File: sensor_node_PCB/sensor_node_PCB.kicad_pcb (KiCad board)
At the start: 2 copper layers, 97.8 x 49 mm, 47 parts, among them J1 USB_B_Mini, J3 OUTPUT_CONNECTOR, P1 BREAKOUTS, Q1 FDN340P, Q2 BSS138, Q3 BSS138, SW1 RESET_SWITCH, U1 LMV358IDGKR, U2 LD1117S50TR, U3 FT231XS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

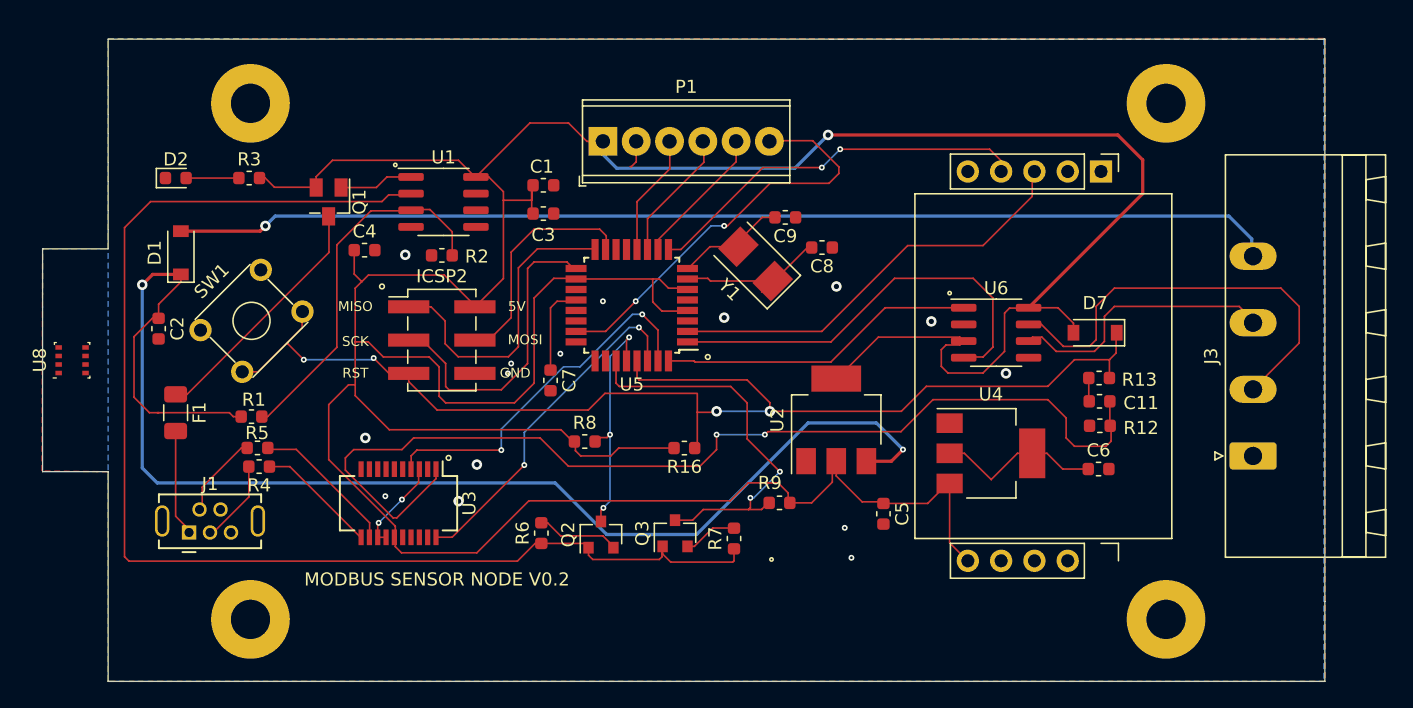
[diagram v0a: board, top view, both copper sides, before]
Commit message: put curved edges on tab
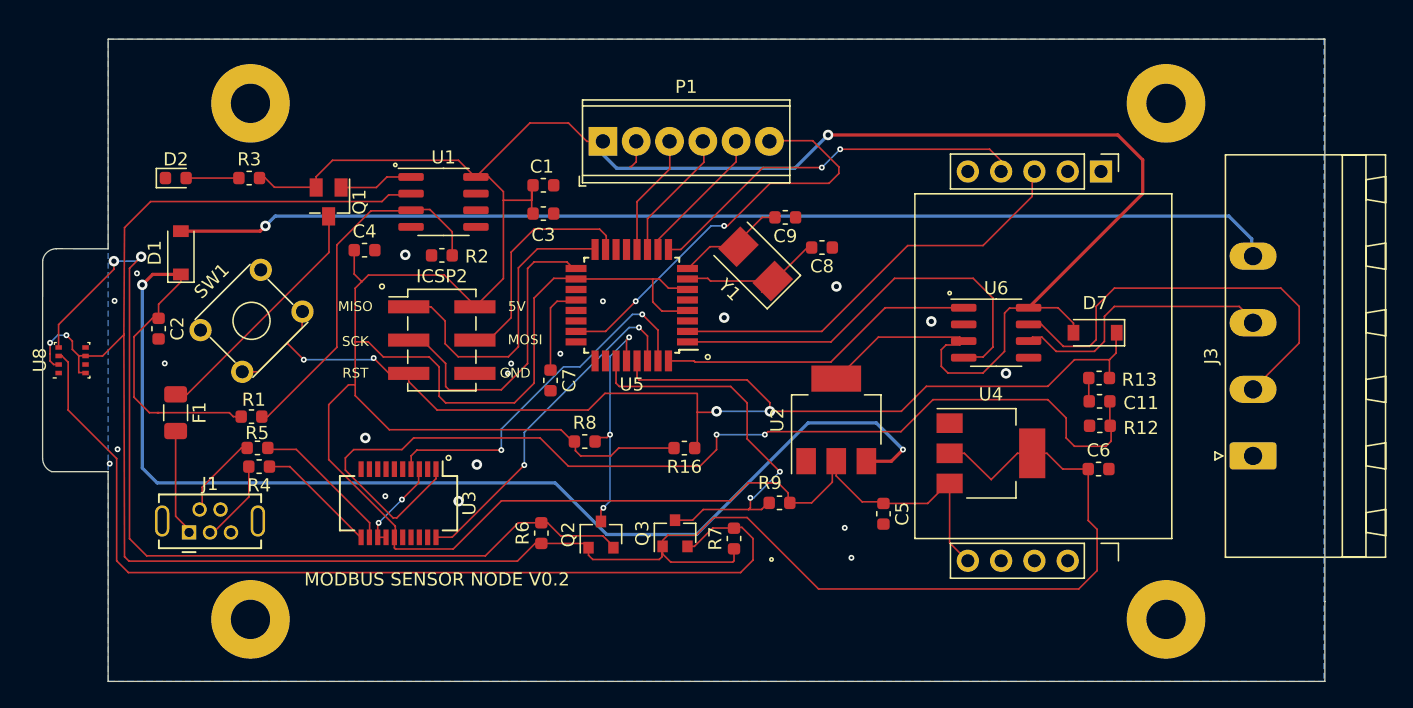
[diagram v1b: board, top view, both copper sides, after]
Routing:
- net /ARD_SDA_3V3: track 4.13 -> 74.5 mm
- net /ARD_SCL_3V3: track 6.25 -> 71.6 mm, vias 0 -> 2
- net 3V3_LDO: track 111.2 -> 167.4 mm, vias 0 -> 2
- net GND: vias 15 -> 20
- removed copper zone on F.Cu, net GND
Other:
- outline, holes or cut-outs redrawn

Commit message: replaced missing gnd plane
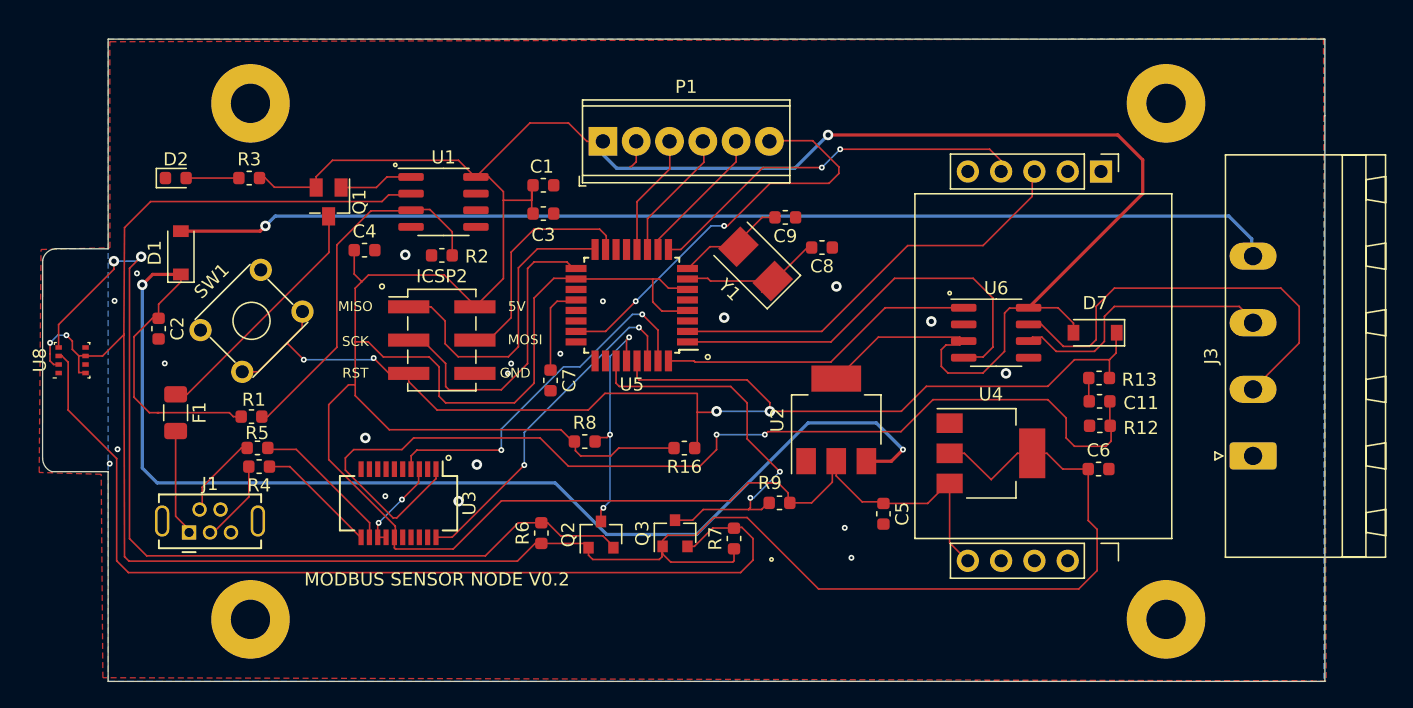
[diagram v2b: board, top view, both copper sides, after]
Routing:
- added copper zone on F.Cu, net GND
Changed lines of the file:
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@@
+    )
+  )
+  (zone (net 2) (net_name GND) (layer F.Cu) (hatch edge 0.508)
+    (connect_pads (clearance 0.254))
+    (min_thickness 0.254)
+    (fill yes (arc_segments 32) (thermal_gap 0.508) (thermal_bridge_width 0.508))
+    (polygon
+      (pts
+        (xy 200.18 132.97) (xy 106.85 132.72) (xy 106.72 117.2) (xy 101.99 117.06) (xy 102.13 100.05)
+        (xy 107.39 99.92) (xy 107.38 84.18) (xy 107.42 84.2) (xy 199.97 83.95)
+      )
     )
   )

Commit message: routed max485 en to ard d8
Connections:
- P1 pad 3: /atmega328p/ARD_DIG8 -> /atmega328p/ARD_DIG9
- U5 pad 12: /atmega328p/ARD_DIG8 -> /RS485_LINE_EN!
- U5 pad 13: Net-(U5-Pad13) -> /atmega328p/ARD_DIG9
- U6 pad 2: GND -> /RS485_LINE_EN!
- U6 pad 3: 5V_LDO -> /RS485_LINE_EN!
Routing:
- net /RS485_LINE_EN!: track 0.00 -> 36.6 mm, vias 0 -> 4
- net /atmega328p/ARD_DIG9: track 0.00 -> 9.43 mm
- net /atmega328p/ARD_DIG8: track 9.19 -> 0.00 mm
- net 5V_LDO: track 298.9 -> 292.3 mm

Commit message: added sht20 to tab
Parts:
- added U9: sht20, Package_DFN_QFN:DFN-6-1EP_3x3mm_P1mm_EP1.5x2.4mm, F.Cu at (104.9, 103.3)
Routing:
- net 3V3_LDO: track 167.4 -> 174.7 mm, vias 2 -> 3
- net /ARD_SDA_3V3: track 74.5 -> 81.7 mm
- net /ARD_SCL_3V3: track 71.6 -> 75.3 mm, vias 2 -> 4
- net GND: vias 20 -> 22
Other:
- board text added: "+12V"
- board text added: "A-"
- board text added: "B+"

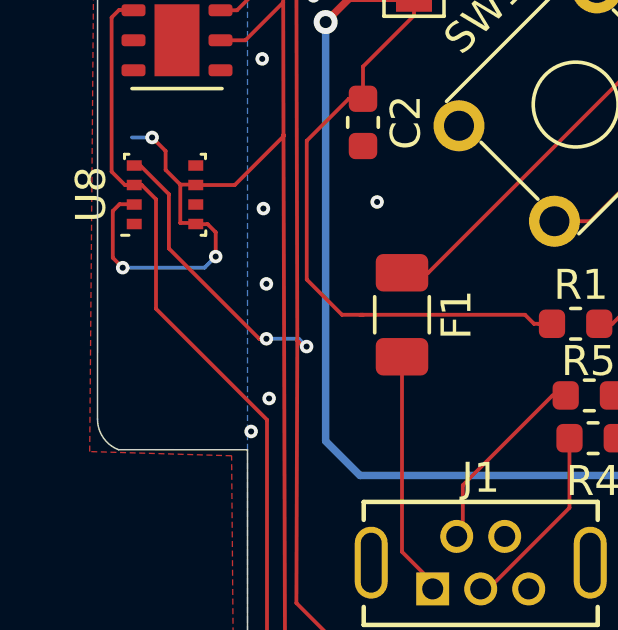
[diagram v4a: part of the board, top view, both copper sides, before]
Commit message: added dps310 to schem and board
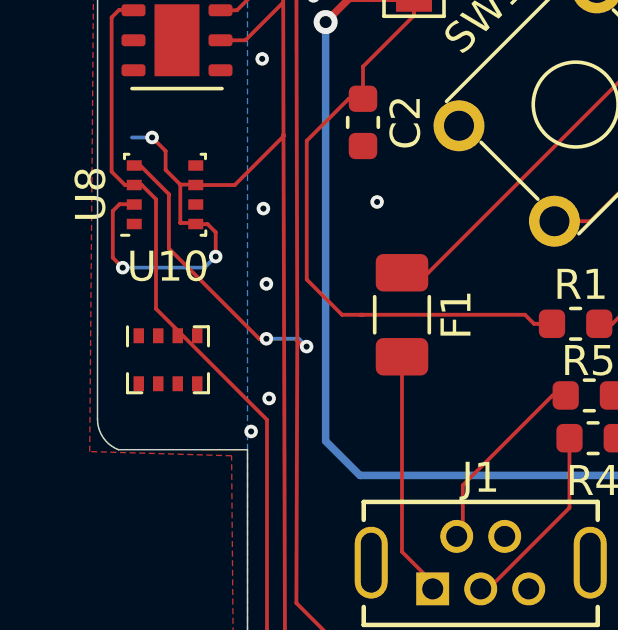
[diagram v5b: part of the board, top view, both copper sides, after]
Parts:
- added U10: dps310, Package_LGA:Bosch_LGA-8_2x2.5mm_P0.65mm_ClockwisePinNumbering, F.Cu at (104.6, 114.0)
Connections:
- U9 pad 7: GND -> Net-(U9-Pad7)
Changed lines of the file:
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@@
     (tracks 558)
     (zones 0)
-    (modules 48)
-    (nets 65)
+    (modules 49)
+    (nets 68)
   )
   (page A4)
@@
   )
   (setup
-    (last_trace_width 0.127)
+    (last_trace_width 0.25)
     (user_trace_width 0.127)
     (user_trace_width 0.5)
@@
   (net 63 "Net-(U9-Pad3)")
   (net 64 "Net-(U9-Pad4)")
+  (net 65 "Net-(U9-Pad7)")
+  (net 66 "Net-(U10-Pad5)")
+  (net 67 "Net-(U10-Pad2)")
   (net_class Default "This is the default net class."
     (clearance 0.2)
@@
     (add_net "Net-(Q1-Pad1)")
     (add_net "Net-(R1-Pad1)")
+    (add_net "Net-(U10-Pad2)")
+    (add_net "Net-(U10-Pad5)")
     (add_net "Net-(U3-Pad10)")
     (add_net "Net-(U3-Pad13)")
@@
     (add_net "Net-(U9-Pad3)")
     (add_net "Net-(U9-Pad4)")
+    (add_net "Net-(U9-Pad7)")
     (add_net USBVCC)
     (add_net Vin)
@@
       (net 23 /ARD_SCL_3V3))
     (pad 7 smd rect (at 0 0) (size 1.5 2.4) (layers F.Cu F.Mask)
-      (net 2 GND))
+      (net 65 "Net-(U9-Pad7)"))
     (pad "" smd roundrect (at -0.375 -0.6) (size 0.6 0.97) (layers F.Paste) (roundrect_rratio 0.25))
     (pad "" smd roundrect (at -0.375 0.6) (size 0.6 0.97) (layers F.Paste) (roundrect_rratio 0.25))
@@
       (at (xyz 0 0 0))
       (scale (xyz 1 1 1))
+      (rotate (xyz 0 0 0))
+    )
+  )
+  (module Package_LGA:Bosch_LGA-8_2x2.5mm_P0.65mm_ClockwisePinNumbering (layer F.Cu)
+    (at 104.6 114)
+    (descr "LGA-8, https://ae-bst.resource.bosch.com/media/_tech/media/datasheets/BST-BMP280-DS001-18.pdf")
+    (tags "lga land grid array")
+    (attr smd)
+    (fp_text reference U10 (at 0 -3.1) (layer F.SilkS)
+      (effects (font (size 1 1) (thickness 0.15)))
+    )
+    (fp_text value dps310 (at 0 3.1) (layer F.Fab)
+      (effects (font (size 1 1) (thickness 0.15)))
+    )
+    (fp_line (start -1.35 1.1) (end -0.87 1.1) (layer F.SilkS) (width 0.1))
+    (fp_text user %R (at 0 0) (layer F.Fab)
+      (effects (font (size 0.5 0.5) (thickness 0.075)))
+    )
+    (fp_line (start -1.55 -1.3) (end 1.55 -1.3) (layer F.CrtYd) (width 0.05))
+    (fp_line (start 1.55 -1.3) (end 1.55 1.3) (layer F.CrtYd) (width 0.05))
+    (fp_line (start 1.55 1.3) (end -1.55 1.3) (layer F.CrtYd) (width 0.05))
+    (fp_line (start -1.55 1.3) (end -1.55 -1.3) (layer F.CrtYd) (width 0.05))
+    (fp_line (start -1.25 1) (end 1.25 1) (layer F.Fab) (width 0.1))
+    (fp_line (start 1.25 -1) (end 1.25 1) (layer F.Fab) (width 0.1))
+    (fp_line (start 1.25 -1) (end -1 -1) (layer F.Fab) (width 0.1))
+    (fp_line (start -1 -1) (end -1.25 -0.75) (layer F.Fab) (width 0.1))
+    (fp_line (start -1.25 1) (end -1.25 -0.75) (layer F.Fab) (width 0.1))
+    (fp_line (start 0.87 1.1) (end 1.35 1.1) (layer F.SilkS) (width 0.1))
+    (fp_line (start 1.35 1.1) (end 1.35 0.46) (layer F.SilkS) (width 0.1))
+    (fp_line (start -1.35 1.1) (end -1.35 0.46) (layer F.SilkS) (width 0.1))
+    (fp_line (start 1.35 -0.46) (end 1.35 -1.1) (layer F.SilkS) (width 0.1))
+    (fp_line (start 0.87 -1.1) (end 1.35 -1.1) (layer F.SilkS) (width 0.1))
+    (fp_line (start -1.35 -0.46) (end -1.35 -1.1) (layer F.SilkS) (width 0.1))
+    (pad 1 smd rect (at -0.975 -0.8 90) (size 0.5 0.35) (layers F.Cu F.Paste F.Mask)
+      (net 2 GND))
+    (pad 5 smd rect (at 0.975 0.8 90) (size 0.5 0.35) (layers F.Cu F.Paste F.Mask)
+      (net 66 "Net-(U10-Pad5)"))
+    (pad 6 smd rect (at 0.325 0.8 90) (size 0.5 0.35) (layers F.Cu F.Paste F.Mask)
+      (net 4 3V3_LDO))
+    (pad 7 smd rect (at -0.325 0.8 90) (size 0.5 0.35) (layers F.Cu F.Paste F.Mask)
+      (net 2 GND))
+    (pad 4 smd rect (at 0.975 -0.8 90) (size 0.5 0.35) (layers F.Cu F.Paste F.Mask)
+      (net 23 /ARD_SCL_3V3))
+    (pad 3 smd rect (at 0.325 -0.8 90) (size 0.5 0.35) (layers F.Cu F.Paste F.Mask)
+      (net 26 /ARD_SDA_3V3))
+    (pad 2 smd rect (at -0.325 -0.8 90) (size 0.5 0.35) (layers F.Cu F.Paste F.Mask)
+      (net 67 "Net-(U10-Pad2)"))
+    (pad 8 smd rect (at -0.975 0.8 90) (size 0.5 0.35) (layers F.Cu F.Paste F.Mask)
+      (net 4 3V3_LDO))
+    (model ${KISYS3DMOD}/Package_LGA.3dshapes/Bosch_LGA-8_2x2.5mm_P0.65mm_ClockwisePinNumbering.wrl
+      (at (xyz 0 0 0))
+      (scale (xyz 1 1 1))

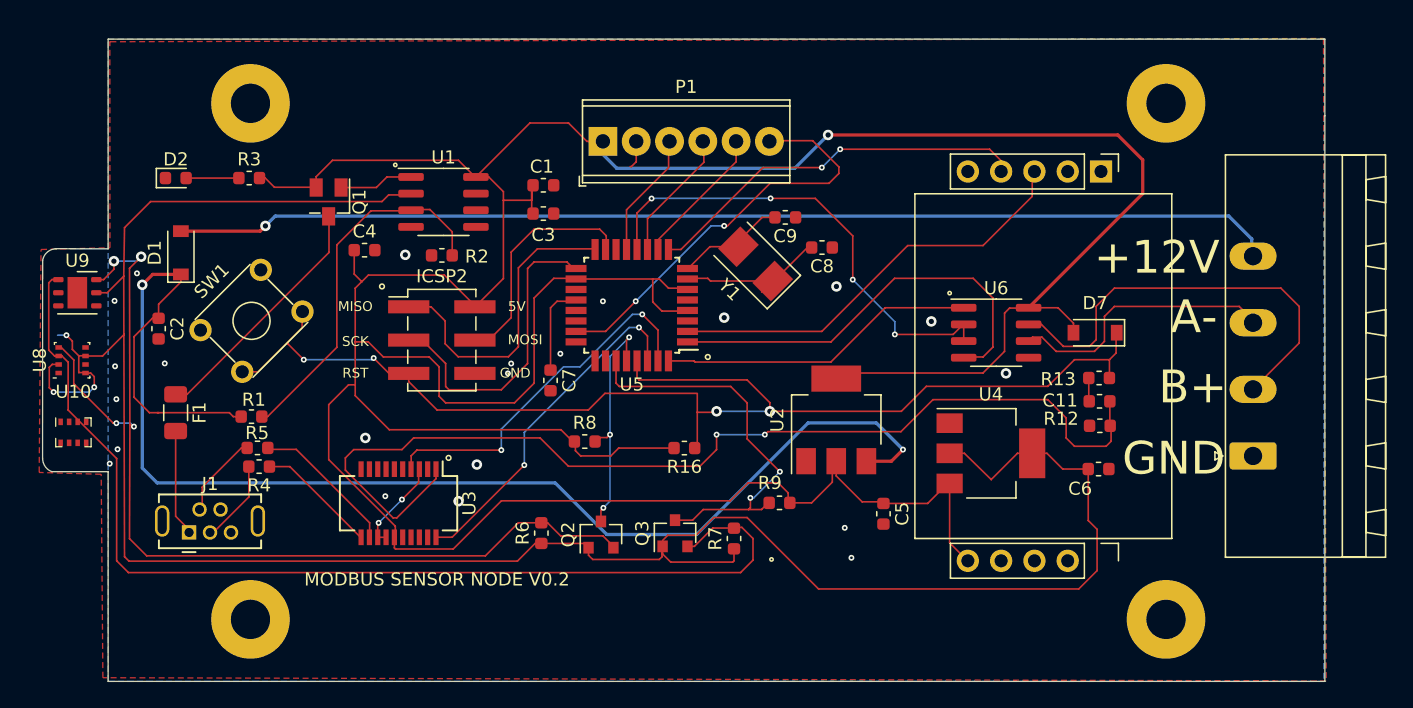
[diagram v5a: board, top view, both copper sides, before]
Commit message: changed term block to 5.08mm - added silk pin labels
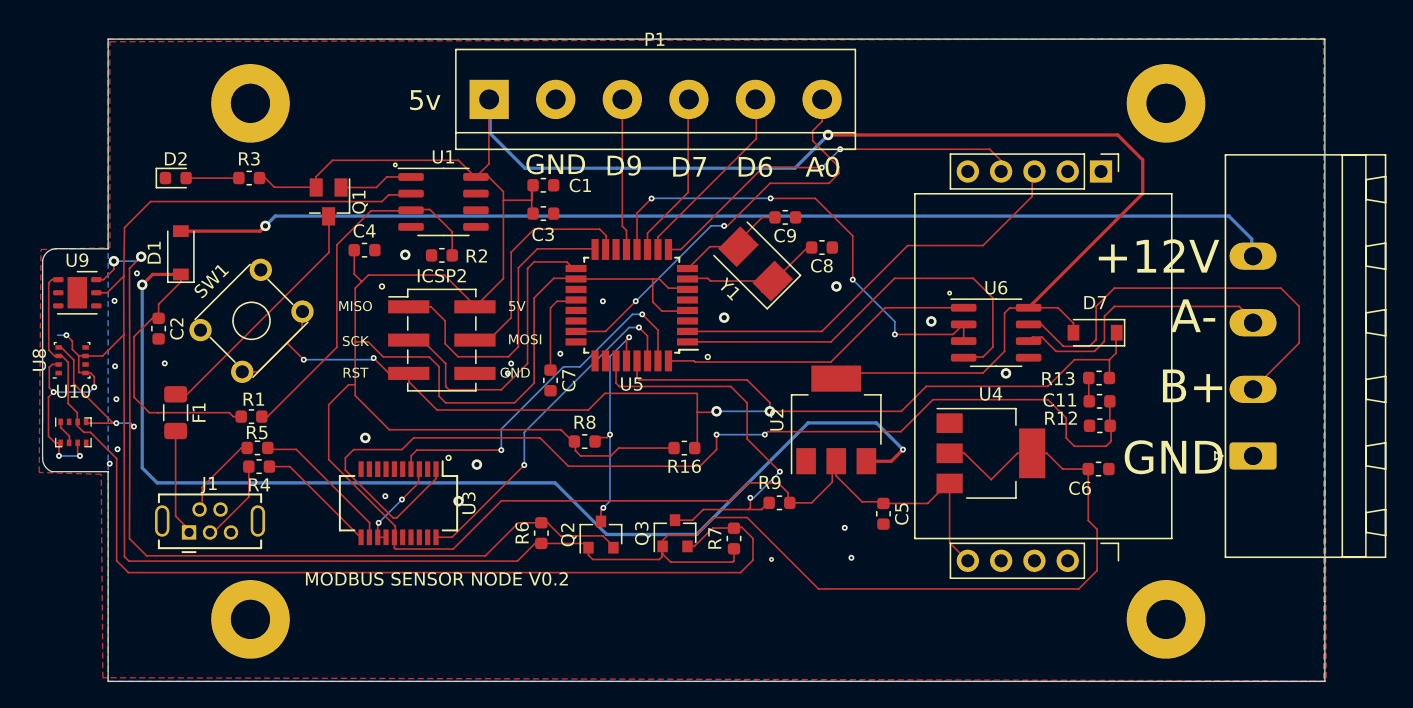
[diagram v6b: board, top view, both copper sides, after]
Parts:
- P1: footprint TerminalBlock_Phoenix:TerminalBlock_Phoenix_MPT-0,5-6-2.54_1x06_P2.54mm_Horizontal -> TerminalBlock:TerminalBlock_bornier-6_P5.08mm
- moved P1 9.25 mm to (136.3, 88.6)
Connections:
- U9 pad 7: Net-(U9-Pad7) -> GND
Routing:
- net 3V3_LDO: track 174.7 -> 183.1 mm, vias 3 -> 5
- net 5V_LDO: track 292.3 -> 297.4 mm
- net /atmega328p/ARD_DIG6: track 10.7 -> 15.2 mm
- net /atmega328p/ARD_DIG7: track 9.93 -> 12.5 mm
- net /ARD_SCL_3V3: track 75.3 -> 77.7 mm
- net /atmega328p/ARD_DIG9: track 9.43 -> 11.6 mm
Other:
- board text added: "5v"
- board text added: "A0"
- board text added: "D6"
- board text added: "D7"
- board text added: "D9"
